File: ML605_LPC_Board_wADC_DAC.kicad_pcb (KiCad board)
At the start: 4 copper layers, 100 x 100 mm, 112 parts, among them IC1 ADC10D040CIVS_NOPB, IC2 AD8137YRZ-REEL, IC3 AD8137YRZ-REEL, IC4 DAC5652IPFB, J1 ASP-134604-01, J10 Conn_02x06_Odd_Even, J11 Conn_02x06_Odd_Even, J12 Conn_02x06_Odd_Even, J13 Conn_01x03_Pin, J14 Conn_01x03_Pin, J2 Conn_01x03_Pin, J3 Conn_01x03_Pin, J4 SMA Connector, J5 SMA Connector, J6 Conn_01x03_Pin, J7 Conn_01x03_Pin, J8 SMA Connector, J9 SMA Connector, U1 LMV7219M7, U2 LMV7219M7, U3 NCV317, U4 LMH6702MA, U5 LMH6702MA

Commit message: Other minor changes
Including removing some unused nets in the schematic, changing L01_P/N back to L01_P/N_CC and adding the Mouser link to the BRD_PRSNT pullup resistor.
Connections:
- net /LA01_N renamed /LA01_N_CC
- net /LA01_P renamed /LA01_P_CC
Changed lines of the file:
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@@
 	(net 171 "Net-(J7-Pin_1)")
 	(net 172 "Net-(J6-Pin_1)")
-	(net 173 "/LA01_P")
-	(net 174 "/LA01_N")
+	(net 173 "/LA01_N_CC")
+	(net 174 "/LA01_P_CC")
 	(footprint "Capacitor_SMD:C_0805_2012Metric_Pad1.18x1.45mm_HandSolder"
 		(layer "F.Cu")
@@
 			)
 		)
+		(property "Mouser Link" "https://ro.mouser.com/ProductDetail/YAGEO/AC0805JR-071KL?qs=sGAEpiMZZMtlubZbdhIBIG07xJe44c5APYMj%2Fj7aA%2Fo%3D"
+			(at 0 0 0)
+			(unlocked yes)
+			(layer "F.Fab")
+			(hide yes)
+			(effects
+				(font
+					(size 1 1)
+					(thickness 0.15)
+				)
+			)
+		)
 		(property ki_fp_filters "R_*")
 		(sheetname "Root")
@@
 			(layers "*.Cu" "*.Mask")
 			(remove_unused_layers no)
-			(net 174 "/LA01_N")
+			(net 173 "/LA01_N_CC")
 			(pinfunction "Pin_3")
 			(pintype "passive")
@@
 			(layers "*.Cu" "*.Mask")
 			(remove_unused_layers no)
-			(net 173 "/LA01_P")
+			(net 174 "/LA01_P_CC")
 			(pinfunction "Pin_4")
 			(pintype "passive")
@@
 			(size 0.64 0.64)
 			(layers "B.Cu" "B.Paste" "B.Mask")
-			(net 173 "/LA01_P")
+			(net 174 "/LA01_P_CC")
 			(pinfunction "D8")
 			(pintype "passive")
@@
 			(size 0.64 0.64)
 			(layers "B.Cu" "B.Paste" "B.Mask")
-			(net 174 "/LA01_N")
+			(net 173 "/LA01_N_CC")
 			(pinfunction "D9")
 			(pintype "passive")
@@
 	)
 	(segment
-		(start 86.535211 108.979001)
-		(end 85.414 110.100212)
+		(start 78.0344 117.7556)
+		(end 76.905 118.885)
 		(width 0.254)
 		(layer "F.Cu")
@@
 	)
 	(segment
-		(start 85.414 114.545212)
-		(end 84.512962 115.44625)
+		(start 84.906 109.889788)
+		(end 84.906 114.334788)
 		(width 0.254)
 		(layer "F.Cu")
@@
 	)
 	(segment
-		(start 83.630288 116.337)
-		(end 83.62625 116.332962)
+		(start 84.149712 115.083)
+		(end 83.630288 115.083)
 		(width 0.254)
 		(layer "F.Cu")
@@
 	)
 	(segment
-		(start 81.074212 118.885)
-		(end 79.445 118.885)
+		(start 83.630288 115.083)
+		(end 83.263 115.450288)
 		(width 0.254)
 		(layer "F.Cu")
@@
 	)
 	(segment
-		(start 87.319001 108.979001)
-		(end 86.535211 108.979001)
+		(start 86.324789 108.470999)
+		(end 84.906 109.889788)
 		(width 0.254)
 		(layer "F.Cu")
@@
 	)
 	(segment
-		(start 84.517 115.450288)
-		(end 84.517 115.969712)
+		(start 84.906 114.334788)
+		(end 84.15375 115.087038)
 		(width 0.254)
 		(layer "F.Cu")
@@
 	)
 	(segment
-		(start 85.414 110.100212)
-		(end 85.414 114.545212)
+		(start 84.15375 115.087038)
+		(end 84.149712 115.083)
 		(width 0.254)
 		(layer "F.Cu")
@@
 	)
 	(segment
-		(start 84.517 115.969712)
-		(end 84.149712 116.337)
+		(start 87.319001 108.470999)
+		(end 86.324789 108.470999)
 		(width 0.254)
 		(layer "F.Cu")
@@
 	)
 	(segment
-		(start 84.512962 115.44625)
-		(end 84.517 115.450288)
+		(start 81.485188 117.7556)
+		(end 78.0344 117.7556)
 		(width 0.254)
 		(layer "F.Cu")
@@
 	)
 	(segment
-		(start 84.149712 116.337)
-		(end 83.630288 116.337)
+		(start 83.263 115.450288)
+		(end 83.263 115.969712)
 		(width 0.254)
 		(layer "F.Cu")
@@
 	)
 	(segment
-		(start 83.62625 116.332962)
-		(end 81.074212 118.885)
+		(start 83.267038 115.97375)
+		(end 81.485188 117.7556)
 		(width 0.254)
 		(layer "F.Cu")
@@
 	)
 	(segment
-		(start 87.7 109.36)
-		(end 87.319001 108.979001)
+		(start 83.263 115.969712)
+		(end 83.267038 115.97375)
+		(width 0.254)
+		(layer "F.Cu")
+		(net 173)
+	)
+	(segment
+		(start 87.7 108.09)
+		(end 87.319001 108.470999)
 		(width 0.254)
 		(layer "F.Cu")
@@
 	)
 	(via
-		(at 87.7 109.36)
+		(at 87.7 108.09)
 		(size 0.6)
 		(drill 0.3)
@@
 	)
 	(segment
-		(start 86.549 109.36)
-		(end 87.581 109.36)
+		(start 86.549 108.09)
+		(end 87.581 108.09)
 		(width 0.508)
 		(layer "B.Cu")
@@
 	)
 	(segment
-		(start 78.0344 117.7556)
-		(end 76.905 118.885)
-		(width 0.254)
-		(layer "F.Cu")
-		(net 174)
-	)
-	(segment
-		(start 84.906 109.889788)
-		(end 84.906 114.334788)
+		(start 86.535211 108.979001)
+		(end 85.414 110.100212)
 		(width 0.254)
 		(layer "F.Cu")
@@
 	)
 	(segment
-		(start 84.149712 115.083)
-		(end 83.630288 115.083)
+		(start 85.414 114.545212)
+		(end 84.512962 115.44625)
 		(width 0.254)
 		(layer "F.Cu")
@@
 	)
 	(segment
-		(start 83.630288 115.083)
-		(end 83.263 115.450288)
+		(start 83.630288 116.337)
+		(end 83.62625 116.332962)
 		(width 0.254)
 		(layer "F.Cu")
@@
 	)
 	(segment
-		(start 86.324789 108.470999)
-		(end 84.906 109.889788)
+		(start 81.074212 118.885)
+		(end 79.445 118.885)
 		(width 0.254)
 		(layer "F.Cu")
@@
 	)
 	(segment
-		(start 84.906 114.334788)
-		(end 84.15375 115.087038)
+		(start 87.319001 108.979001)
+		(end 86.535211 108.979001)
 		(width 0.254)
 		(layer "F.Cu")
@@
 	)
 	(segment
-		(start 84.15375 115.087038)
-		(end 84.149712 115.083)
+		(start 84.517 115.450288)
+		(end 84.517 115.969712)
 		(width 0.254)
 		(layer "F.Cu")
@@
 	)
 	(segment
-		(start 87.319001 108.470999)
-		(end 86.324789 108.470999)
+		(start 85.414 110.100212)
+		(end 85.414 114.545212)
 		(width 0.254)
 		(layer "F.Cu")
@@
 	)
 	(segment
-		(start 81.485188 117.7556)
-		(end 78.0344 117.7556)
+		(start 84.517 115.969712)
+		(end 84.149712 116.337)
 		(width 0.254)
 		(layer "F.Cu")
@@
 	)
 	(segment
-		(start 83.263 115.450288)
-		(end 83.263 115.969712)
+		(start 84.512962 115.44625)
+		(end 84.517 115.450288)
 		(width 0.254)
 		(layer "F.Cu")
@@
 	)
 	(segment
-		(start 83.267038 115.97375)
-		(end 81.485188 117.7556)
+		(start 84.149712 116.337)
+		(end 83.630288 116.337)
 		(width 0.254)
 		(layer "F.Cu")
@@
 	)
 	(segment
-		(start 83.263 115.969712)
-		(end 83.267038 115.97375)
+		(start 83.62625 116.332962)
+		(end 81.074212 118.885)
 		(width 0.254)
 		(layer "F.Cu")
@@
 	)
 	(segment
-		(start 87.7 108.09)
-		(end 87.319001 108.470999)
+		(start 87.7 109.36)
+		(end 87.319001 108.979001)
 		(width 0.254)
 		(layer "F.Cu")
@@
 	)
 	(via
-		(at 87.7 108.09)
+		(at 87.7 109.36)
 		(size 0.6)
 		(drill 0.3)
@@
 	)
 	(segment
-		(start 86.549 108.09)
-		(end 87.581 108.09)
+		(start 86.549 109.36)
+		(end 87.581 109.36)
 		(width 0.508)
 		(layer "B.Cu")

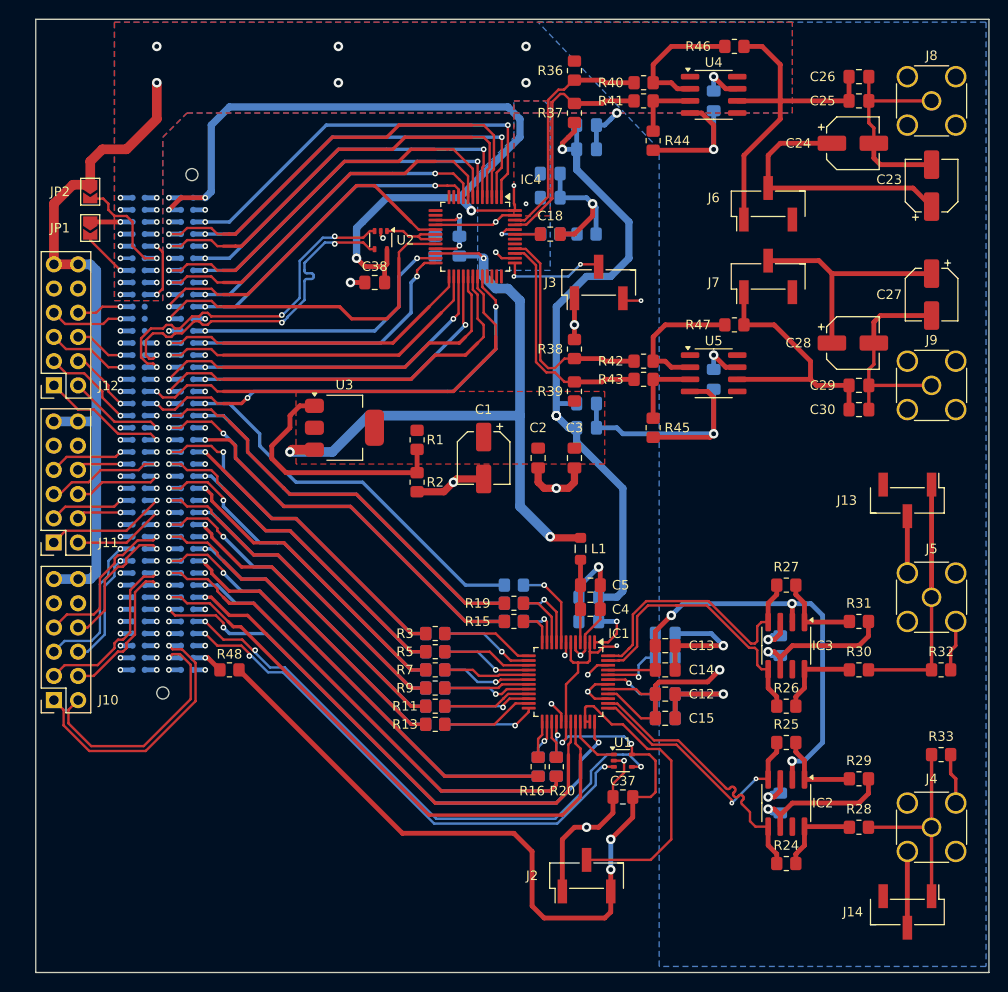
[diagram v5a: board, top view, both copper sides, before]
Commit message: Added some silkscreen markings
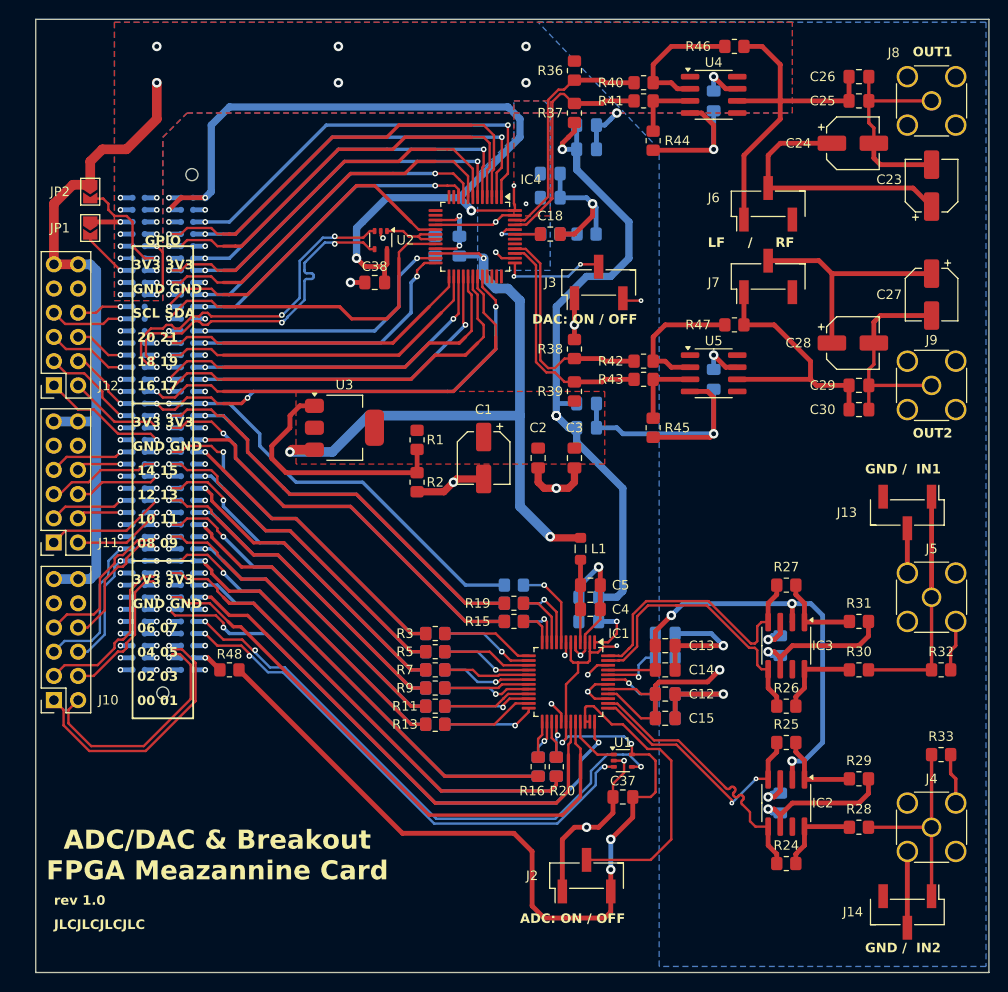
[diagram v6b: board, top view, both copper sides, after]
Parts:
- moved J13 1.27 mm to (166.4, 101.7)
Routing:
- net /ADC_Circuit/I_IN: track 26.1 -> 24.8 mm
- net GNDA: track 310.6 -> 309.3 mm
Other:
- board text added: "00 01"
- board text added: "02 03"
- board text added: "04 05"
- board text added: "06 07"
- board text added: "08 09"
- board text added: "10 11"
- board text added: "12 13"
- board text added: "14 15"
- board text added: "16 17"
- board text added: "18 19"
- board text added: "20 21"
- board text added: "3V3 3V3"
- board text added: "ADC/DAC & Breakout FPGA Meazannine Card"
- board text added: "ADC: ON / OFF"
- board text added: "DAC: ON / OFF"
- board text added: "GND / IN1"
- board text added: "GND / IN2"
- board text added: "GND GND"
- board text added: "GPIO"
- board text added: "JLCJLCJLCJLC"
- board text added: "LF / RF"
- board text added: "OUT1"
- board text added: "OUT2"
- board text added: "SCL SDA"
- board text added: "rev 1.0"
